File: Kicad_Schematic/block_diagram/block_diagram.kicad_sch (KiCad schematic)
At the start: 8 parts

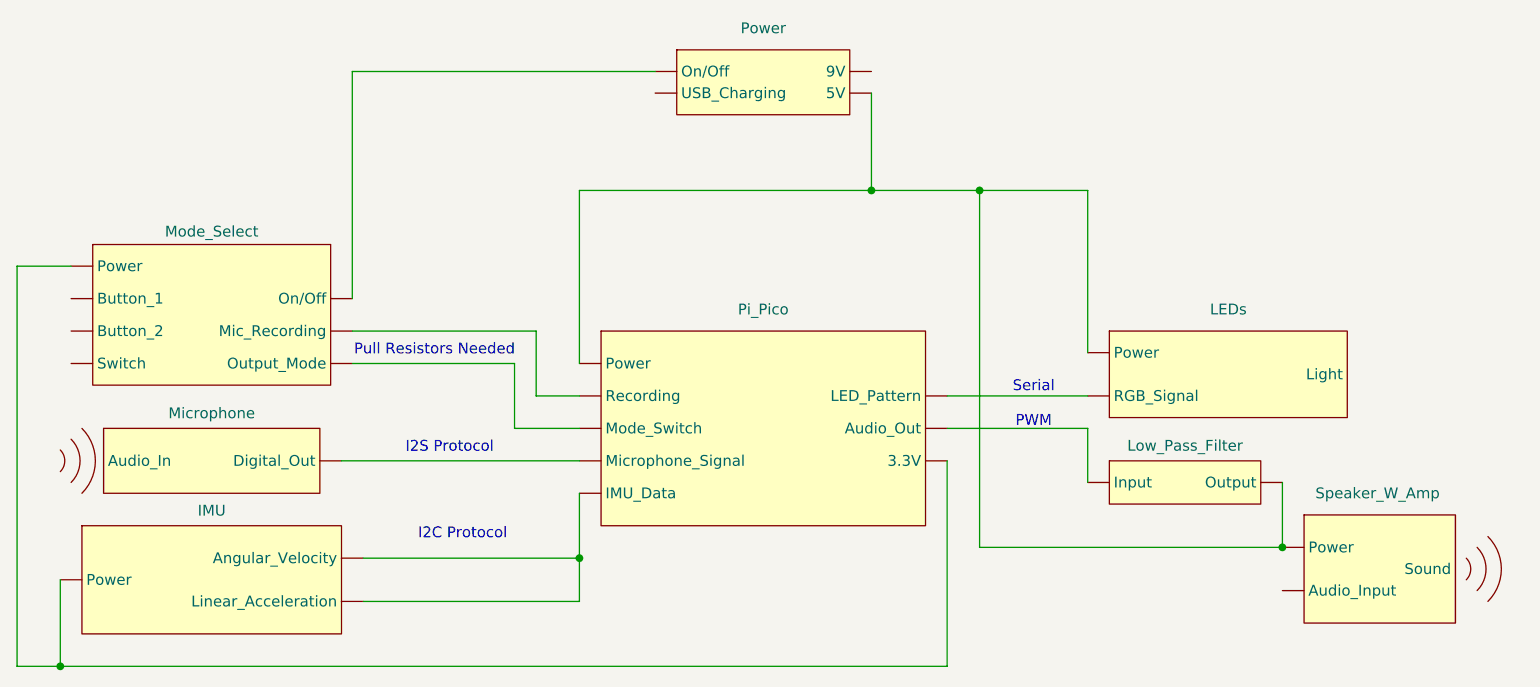
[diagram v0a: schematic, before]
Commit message: Changed on/off switch representation
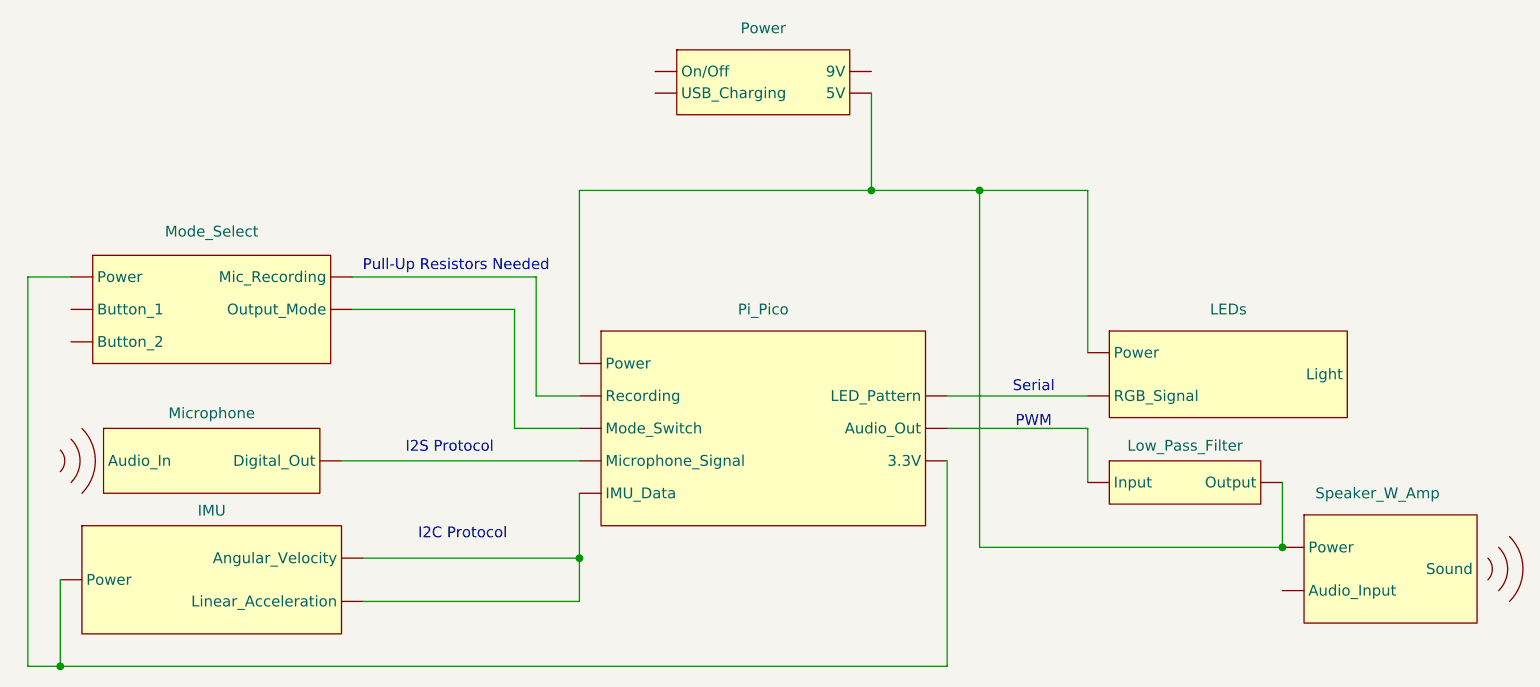
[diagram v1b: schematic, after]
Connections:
- net at LEDs. (Light): now also Pi_Pico. (3.3V)
- net at Pi_Pico. (3.3V): now also Microphone. (Digital_Out); no longer LEDs. (Light)
- net at Mode_Select. (Output_Mode): no longer Pi_Pico. (3.3V)
- net at Microphone. (Digital_Out): no longer Pi_Pico. (3.3V)
- net at Power. (5V): no longer Mode_Select. (Output_Mode)
- new net: LEDs. (Light), Low_Pass_Filter. (Output), Pi_Pico. (3.3V), Power. (5V), Speaker_W_Amp. (Sound)
- new net: Mode_Select. (Output_Mode), Pi_Pico. (3.3V) (x2)
- new net: IMU. (Linear_Acceleration), Mode_Select. (Output_Mode), Pi_Pico. (3.3V)
- now unconnected: Mode_Select. (Output_Mode), Mode_Select. (Output_Mode), Power. (5V), Speaker_W_Amp. (Sound)
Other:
- note added: "Pull-Up Resistors Needed"
- note removed: "Pull Resistors Needed"
- moved on the sheet: Speaker_W_Amp
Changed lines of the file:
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@@
 		)
 	)
-	(text "Pull Resistors Needed\n"
-		(exclude_from_sim no)
-		(at 93.472 93.726 0)
+	(text "Pull-Up Resistors Needed\n"
+		(exclude_from_sim no)
+		(at 96.012 83.82 0)
 		(effects
 			(font
@@
 	(wire
 		(pts
+			(xy 45.72 85.09) (xy 45.72 130.81)
+		)
+		(stroke
+			(width 0)
+			(type default)
+		)
+	)
+	(wire
+		(pts
 			(xy 157.48 74.93) (xy 157.48 116.84)
 		)
@@
 	(wire
 		(pts
+			(xy 83.82 85.09) (xy 105.41 85.09)
+		)
+		(stroke
+			(width 0)
+			(type default)
+		)
+	)
+	(wire
+		(pts
 			(xy 85.09 118.11) (xy 110.49 118.11)
 		)
@@
 	(wire
 		(pts
-			(xy 102.87 95.25) (xy 102.87 102.87)
-		)
-		(stroke
-			(width 0)
-			(type default)
-		)
-	)
-	(wire
-		(pts
-			(xy 49.53 130.81) (xy 44.45 130.81)
-		)
-		(stroke
-			(width 0)
-			(type default)
-		)
-	)
-	(wire
-		(pts
-			(xy 105.41 91.44) (xy 105.41 99.06)
+			(xy 102.87 88.9) (xy 102.87 102.87)
+		)
+		(stroke
+			(width 0)
+			(type default)
+		)
+	)
+	(wire
+		(pts
+			(xy 49.53 130.81) (xy 45.72 130.81)
+		)
+		(stroke
+			(width 0)
+			(type default)
+		)
+	)
+	(wire
+		(pts
+			(xy 83.82 88.9) (xy 102.87 88.9)
+		)
+		(stroke
+			(width 0)
+			(type default)
+		)
+	)
+	(wire
+		(pts
+			(xy 105.41 85.09) (xy 105.41 99.06)
 		)
 		(stroke
@@
 	(wire
 		(pts
-			(xy 44.45 83.82) (xy 50.8 83.82)
-		)
-		(stroke
-			(width 0)
-			(type default)
-		)
-	)
-	(wire
-		(pts
 			(xy 49.53 130.81) (xy 49.53 120.65)
 		)
@@
 	(wire
 		(pts
-			(xy 83.82 87.63) (xy 83.82 60.96)
-		)
-		(stroke
-			(width 0)
-			(type default)
-		)
-	)
-	(wire
-		(pts
-			(xy 83.82 95.25) (xy 102.87 95.25)
-		)
-		(stroke
-			(width 0)
-			(type default)
-		)
-	)
-	(wire
-		(pts
 			(xy 153.67 130.81) (xy 49.53 130.81)
 		)
@@
 	(wire
 		(pts
-			(xy 44.45 130.81) (xy 44.45 83.82)
-		)
-		(stroke
-			(width 0)
-			(type default)
-		)
-	)
-	(wire
-		(pts
 			(xy 157.48 116.84) (xy 193.04 116.84)
 		)
@@
 	(wire
 		(pts
+			(xy 50.8 85.09) (xy 45.72 85.09)
+		)
+		(stroke
+			(width 0)
+			(type default)
+		)
+	)
+	(wire
+		(pts
 			(xy 105.41 99.06) (xy 110.49 99.06)
 		)
@@
 		(pts
 			(xy 110.49 118.11) (xy 110.49 123.19)
-		)
-		(stroke
-			(width 0)
-			(type default)
-		)
-	)
-	(wire
-		(pts
-			(xy 83.82 91.44) (xy 105.41 91.44)
-		)
-		(stroke
-			(width 0)
-			(type default)
-		)
-	)
-	(wire
-		(pts
-			(xy 83.82 60.96) (xy 119.38 60.96)
 		)
 		(stroke
@@
 		)
 		(pin ""
-		)
-		(pin ""
-		)
-		(pin ""

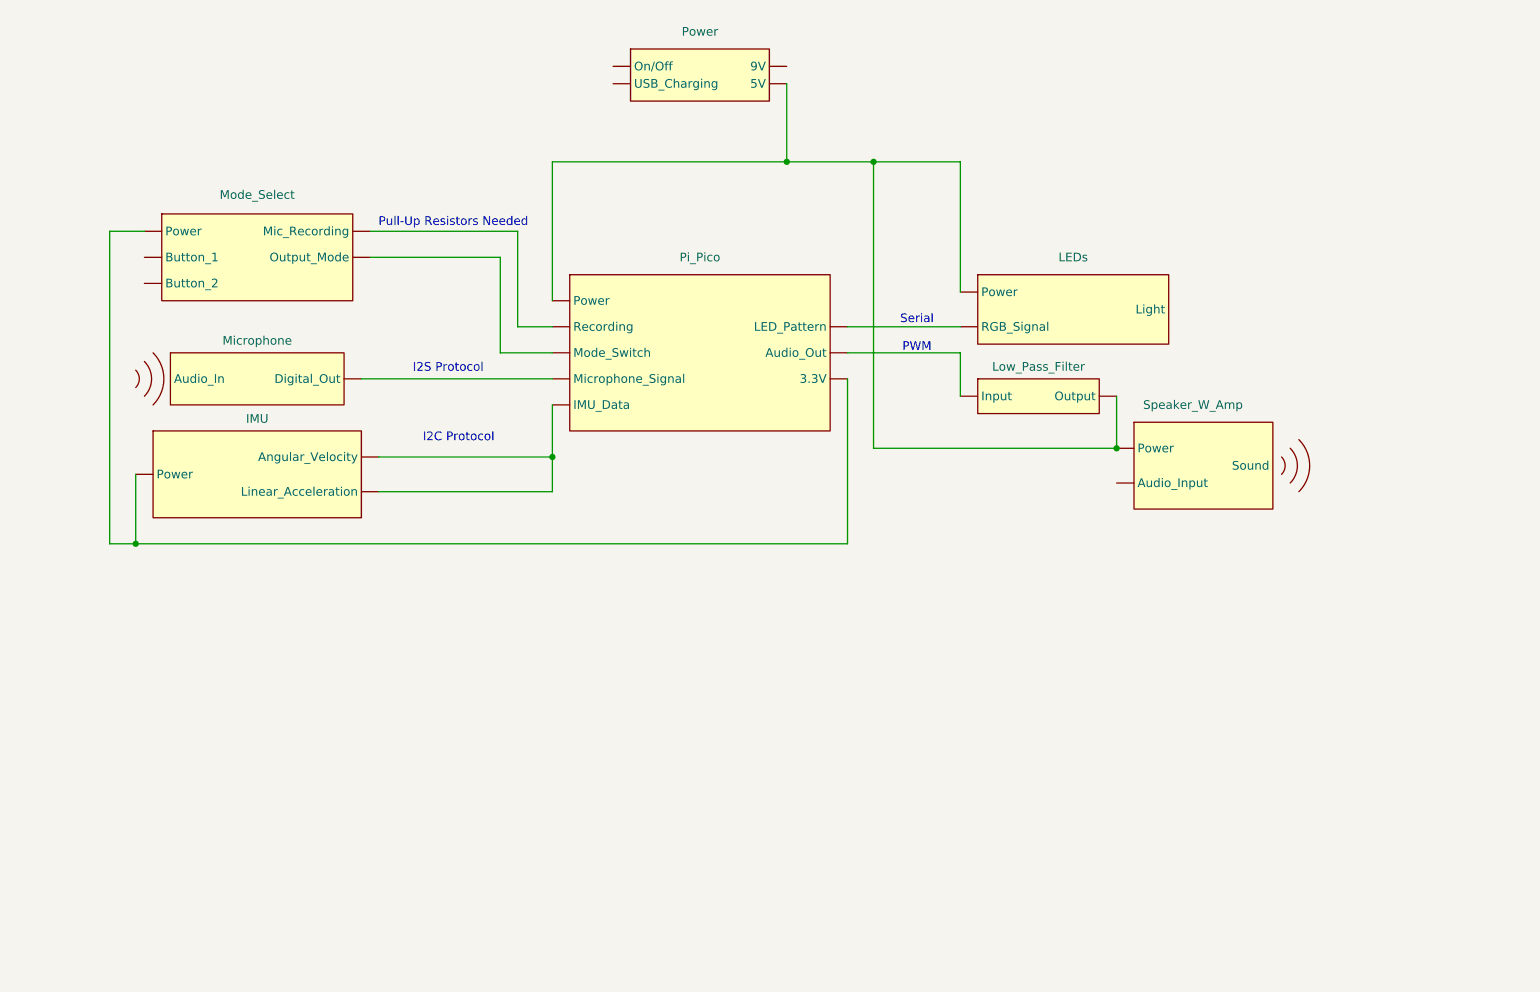
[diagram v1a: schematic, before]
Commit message: Changed block title font size
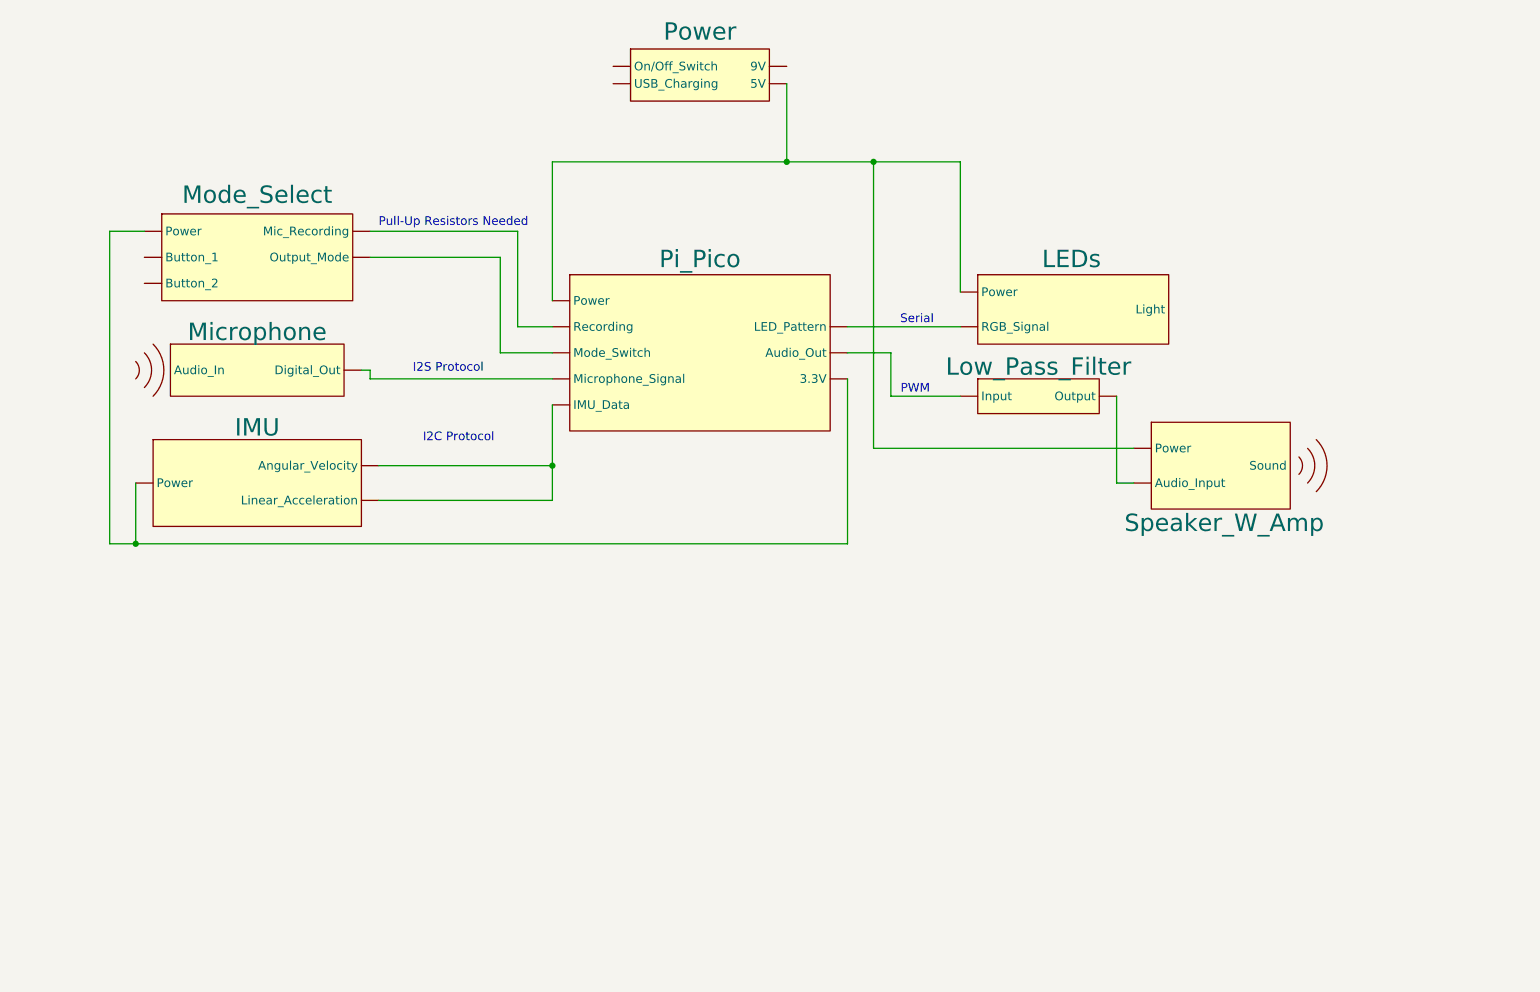
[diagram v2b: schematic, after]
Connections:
- net at Low_Pass_Filter. (Output): now also Speaker_W_Amp. (Sound); no longer Pi_Pico. (3.3V)
- net at LEDs. (Light): now also Pi_Pico. (3.3V), Power. (5V), Speaker_W_Amp. (Sound)
- net at Pi_Pico. (3.3V): now also Microphone. (Digital_Out); no longer LEDs. (Light)
- net at Mode_Select. (Output_Mode): no longer Pi_Pico. (3.3V)
- net at Microphone. (Digital_Out): no longer Pi_Pico. (3.3V)
- new net: Low_Pass_Filter. (Output), Pi_Pico. (3.3V)
- new net: LEDs. (Light), Pi_Pico. (3.3V)
- new net: Mode_Select. (Output_Mode), Pi_Pico. (3.3V) (x2)
- new net: IMU. (Linear_Acceleration), Mode_Select. (Output_Mode), Pi_Pico. (3.3V)
- now unconnected: Mode_Select. (Output_Mode), Mode_Select. (Output_Mode), Power. (5V), Speaker_W_Amp. (Sound)
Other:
- moved on the sheet: IMU, Microphone, Speaker_W_Amp
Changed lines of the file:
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@@
 	(text "PWM\n"
 		(exclude_from_sim no)
-		(at 163.83 102.108 0)
+		(at 163.576 108.204 0)
 		(effects
 			(font
@@
 	)
 	(junction
-		(at 193.04 116.84)
-		(diameter 0)
-		(color 0 0 0 0)
-	)
-	(junction
-		(at 110.49 118.11)
-		(diameter 0)
-		(color 0 0 0 0)
-	)
-	(junction
 		(at 157.48 74.93)
 		(diameter 0)
@@
 	)
 	(junction
+		(at 110.49 119.38)
+		(diameter 0)
+		(color 0 0 0 0)
+	)
+	(junction
 		(at 49.53 130.81)
 		(diameter 0)
@@
 	(wire
 		(pts
+			(xy 160.02 102.87) (xy 153.67 102.87)
+		)
+		(stroke
+			(width 0)
+			(type default)
+		)
+	)
+	(wire
+		(pts
 			(xy 144.78 63.5) (xy 144.78 74.93)
 		)
@@
 	(wire
 		(pts
-			(xy 85.09 118.11) (xy 110.49 118.11)
+			(xy 85.09 119.38) (xy 110.49 119.38)
 		)
 		(stroke
@@
 	(wire
 		(pts
+			(xy 160.02 109.22) (xy 160.02 102.87)
+		)
+		(stroke
+			(width 0)
+			(type default)
+		)
+	)
+	(wire
+		(pts
 			(xy 83.82 88.9) (xy 102.87 88.9)
 		)
@@
 	(wire
 		(pts
-			(xy 85.09 123.19) (xy 110.49 123.19)
+			(xy 85.09 124.46) (xy 110.49 124.46)
 		)
 		(stroke
@@
 	(wire
 		(pts
-			(xy 49.53 130.81) (xy 49.53 120.65)
+			(xy 83.82 105.41) (xy 83.82 106.68)
+		)
+		(stroke
+			(width 0)
+			(type default)
+		)
+	)
+	(wire
+		(pts
+			(xy 170.18 109.22) (xy 160.02 109.22)
+		)
+		(stroke
+			(width 0)
+			(type default)
+		)
+	)
+	(wire
+		(pts
+			(xy 49.53 130.81) (xy 49.53 121.92)
 		)
 		(stroke
@@
 	(wire
 		(pts
-			(xy 193.04 109.22) (xy 193.04 116.84)
-		)
-		(stroke
-			(width 0)
-			(type default)
-		)
-	)
-	(wire
-		(pts
 			(xy 153.67 99.06) (xy 170.18 99.06)
 		)
@@
 	(wire
 		(pts
-			(xy 153.67 102.87) (xy 170.18 102.87)
-		)
-		(stroke
-			(width 0)
-			(type default)
-		)
-	)
-	(wire
-		(pts
 			(xy 170.18 74.93) (xy 170.18 93.98)
 		)
@@
 	(wire
 		(pts
-			(xy 170.18 102.87) (xy 170.18 109.22)
-		)
-		(stroke
-			(width 0)
-			(type default)
-		)
-	)
-	(wire
-		(pts
-			(xy 157.48 116.84) (xy 193.04 116.84)
+			(xy 193.04 109.22) (xy 193.04 121.92)
+		)
+		(stroke
+			(width 0)
+			(type default)
+		)
+	)
+	(wire
+		(pts
+			(xy 157.48 116.84) (xy 195.58 116.84)
 		)
 		(stroke
@@
 	(wire
 		(pts
+			(xy 83.82 106.68) (xy 110.49 106.68)
+		)
+		(stroke
+			(width 0)
+			(type default)
+		)
+	)
+	(wire
+		(pts
 			(xy 105.41 99.06) (xy 110.49 99.06)
 		)
@@
 	(wire
 		(pts
-			(xy 110.49 118.11) (xy 110.49 123.19)
-		)
-		(stroke
-			(width 0)
-			(type default)
-		)
-	)
-	(wire
-		(pts
-			(xy 82.55 106.68) (xy 110.49 106.68)
+			(xy 110.49 110.49) (xy 110.49 119.38)
+		)
+		(stroke
+			(width 0)
+			(type default)
+		)
+	)
+	(wire
+		(pts
+			(xy 110.49 119.38) (xy 110.49 124.46)
+		)
+		(stroke
+			(width 0)
+			(type default)
+		)
+	)
+	(wire
+		(pts
+			(xy 82.55 105.41) (xy 83.82 105.41)
 		)
 		(stroke
@@
 	(wire
 		(pts
-			(xy 110.49 110.49) (xy 110.49 118.11)
+			(xy 193.04 121.92) (xy 195.58 121.92)
 		)
 		(stroke
@@
 			(effects
 				(font
-					(size 1.27 1.27)
+					(size 2.54 2.54)
 				)
 			)
@@
 		(on_board yes)
 		(dnp no)
-		(fields_autoplaced yes)
 		(property "Reference" "LEDs"
-			(at 186.69 88.9 0)
-			(effects
-				(font
-					(size 1.27 1.27)
+			(at 186.436 89.154 0)
+			(effects
+				(font
+					(size 2.54 2.54)
 				)
 			)
@@
 		(on_board yes)
 		(dnp no)
-		(fields_autoplaced yes)
 		(property "Reference" "Pi_Pico"
-			(at 132.08 88.9 0)
-			(effects
-				(font
-					(size 1.27 1.27)
+			(at 132.08 89.154 0)
+			(effects
+				(font
+					(size 2.54 2.54)
 				)
 			)
@@
 			(effects
 				(font
-					(size 1.27 1.27)
+					(size 2.54 2.54)
 				)
 			)
@@
 	(symbol
 		(lib_id "Block_Diagram_Blocks:IMU")
-		(at 67.31 127 0)
+		(at 67.31 128.27 0)
 		(unit 1)
 		(exclude_from_sim no)
@@
 		(dnp no)
 		(property "Reference" "IMU"
-			(at 67.31 112.522 0)
-			(effects
-				(font
-					(size 1.27 1.27)
+			(at 67.31 113.792 0)
+			(effects
+				(font
+					(size 2.54 2.54)
 				)
 			)
 		)
 		(property "Value" "~"
-			(at 67.31 111.76 0)
+			(at 67.31 113.03 0)
 			(effects
 				(font
@@
 		)
 		(property "Footprint" ""
-			(at 67.31 127 0)
+			(at 67.31 128.27 0)
 			(effects
 				(font
@@
 		)
 		(property "Datasheet" ""
-			(at 67.31 127 0)
+			(at 67.31 128.27 0)
 			(effects
 				(font
@@
 		)
 		(property "Description" ""
-			(at 67.31 127 0)
+			(at 67.31 128.27 0)
 			(effects
 				(font
@@
 		(on_board yes)
 		(dnp no)
-		(fields_autoplaced yes)
 		(property "Reference" "Power"
 			(at 132.08 55.88 0)
 			(effects
 				(font
-					(size 1.27 1.27)
+					(size 2.54 2.54)
 				)
 			)
@@
 	(symbol
 		(lib_id "Block_Diagram_Blocks:Microphone")
-		(at 67.31 110.49 0)
+		(at 67.31 109.22 0)
 		(unit 1)
 		(exclude_from_sim no)
@@
 		(dnp no)
 		(property "Reference" "Microphone"
-			(at 67.31 101.092 0)
-			(effects
-				(font
-					(size 1.27 1.27)
+			(at 67.31 99.822 0)
+			(effects
+				(font
+					(size 2.54 2.54)
 				)
 			)
 		)
 		(property "Value" "~"
-			(at 64.77 100.33 0)
+			(at 64.77 99.06 0)
 			(effects
 				(font
@@
 		)
 		(property "Footprint" ""
-			(at 67.31 110.49 0)
+			(at 67.31 109.22 0)
 			(effects
 				(font
@@
 		)
 		(property "Datasheet" ""
-			(at 67.31 110.49 0)
+			(at 67.31 109.22 0)
 			(effects
 				(font
@@
 		)
 		(property "Description" ""
-			(at 67.31 110.49 0)
+			(at 67.31 109.22 0)
 			(effects
 				(font
@@
 	(symbol
 		(lib_id "Block_Diagram_Blocks:Speaker_w_Amp")
-		(at 204.47 125.73 0)
+		(at 207.01 125.73 0)
 		(unit 1)
 		(exclude_from_sim no)
@@
 		(dnp no)
 		(property "Reference" "Speaker_W_Amp"
-			(at 204.216 110.49 0)
-			(effects
-				(font
-					(size 1.27 1.27)
+			(at 208.788 127.762 0)
+			(effects
+				(font
+					(size 2.54 2.54)
 				)
 			)
 		)
 		(property "Value" "~"
-			(at 205.8941 110.49 0)
+			(at 208.4341 110.49 0)
 			(effects
 				(font
@@
 		)
 		(property "Footprint" ""
-			(at 204.47 125.73 0)
+			(at 207.01 125.73 0)
 			(effects
 				(font
@@
 		)
 		(property "Datasheet" ""
-			(at 204.47 125.73 0)
+			(at 207.01 125.73 0)
 			(effects
 				(font
@@
 		)
 		(property "Description" ""
-			(at 204.47 125.73 0)
-			(effects
-				(font
+			(at 207.01 125.73 0)
+			(effects
+				(font
